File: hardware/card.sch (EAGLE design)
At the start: 56 parts, among them J1 UE27AC54100, J2 B2PS-VH(LF)(SN), J3 MINI-USB-UX60A-MB-5ST, J4 MICROSD, U1 ATSAMD21J_QFN, U3 TLV70233DBVR, U4 ATWINC1500_MR210PA, U5 NHD-C12832A1Z-FSW-FBW-3V3, U6 MIC2288YD5-TR, X3 32.768

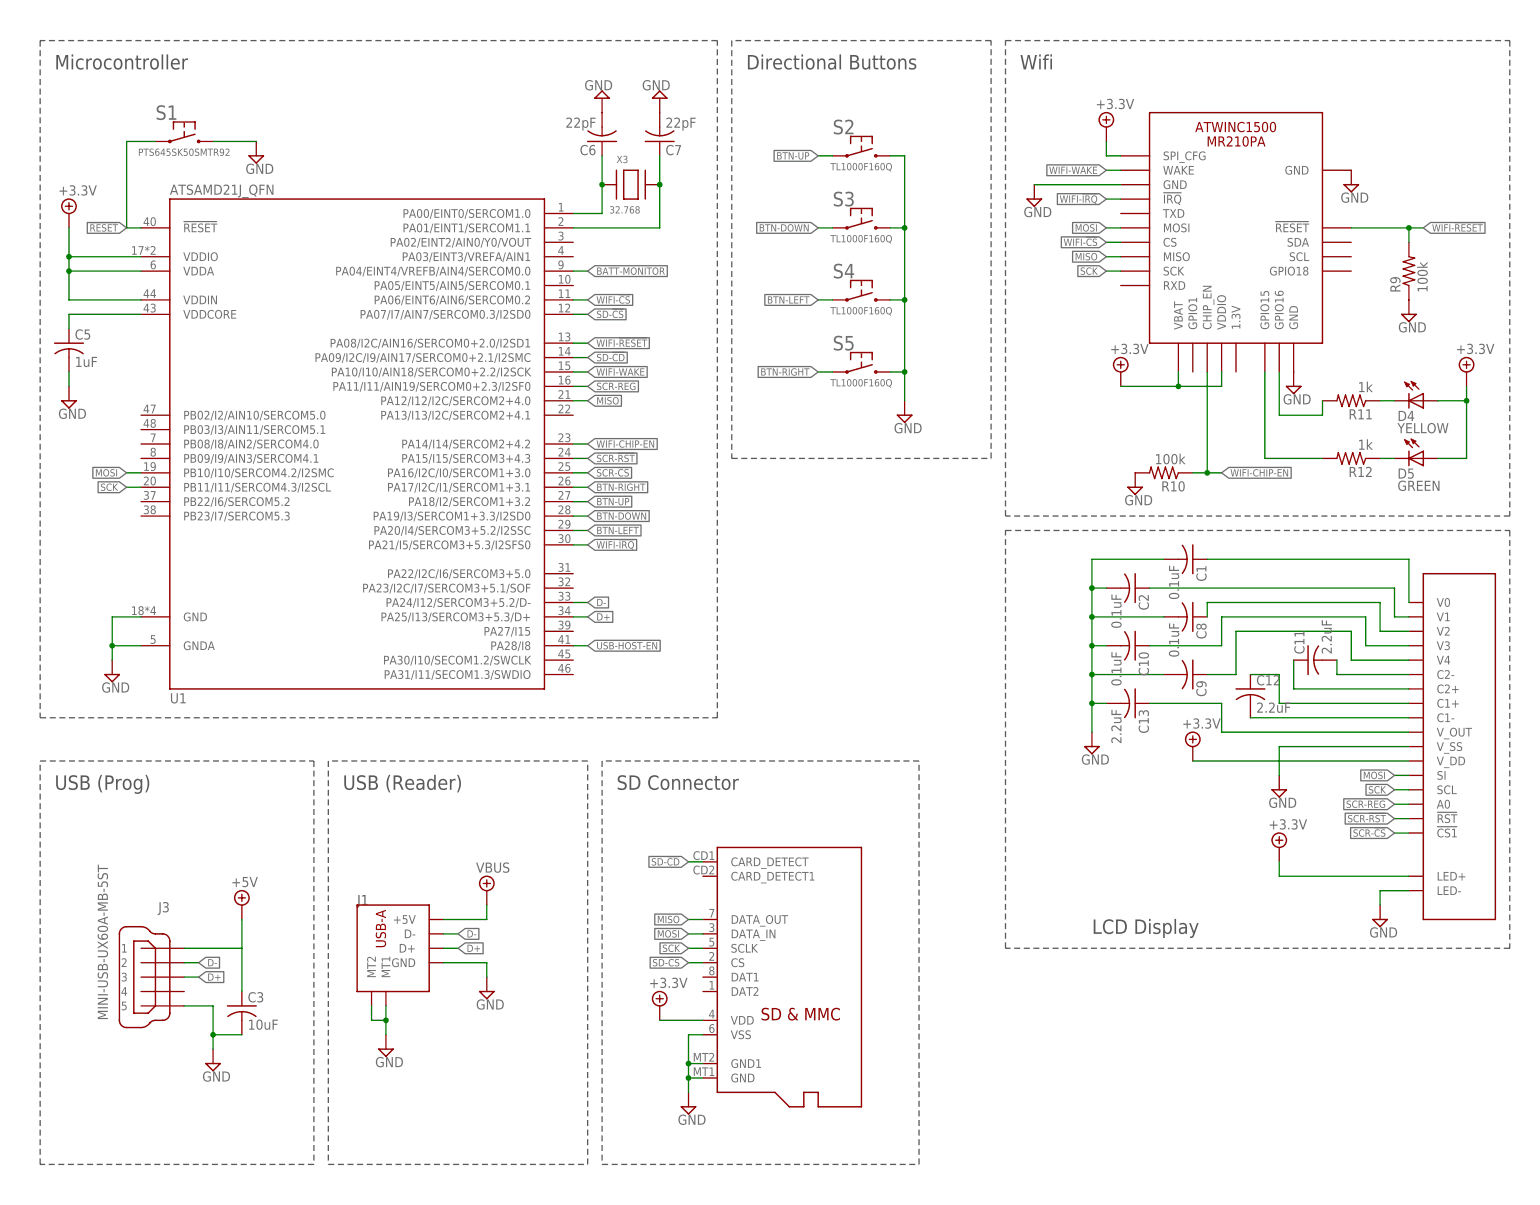
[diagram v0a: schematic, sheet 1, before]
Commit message: add framing for software components. Design review schematic tweaks
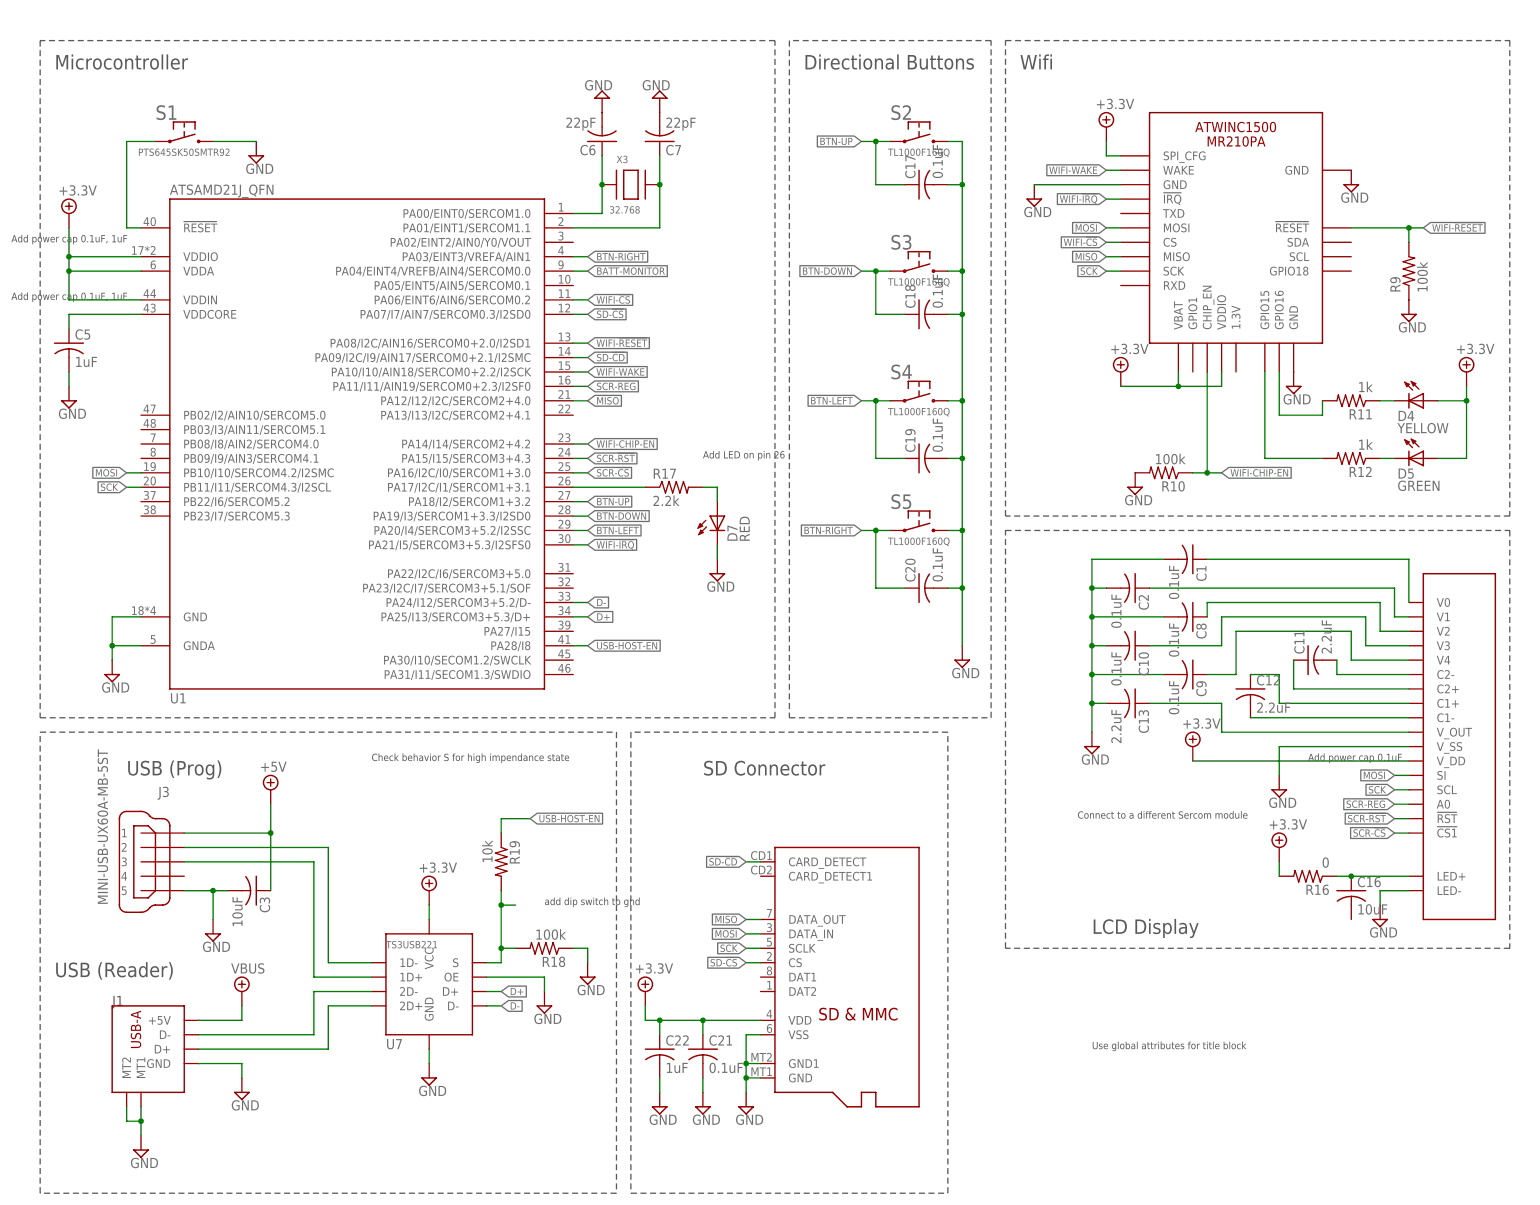
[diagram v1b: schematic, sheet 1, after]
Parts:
- removed CN1: (no value), lib-card:JST_2PIN
- removed T1: (no value), CardReader:BSS138
- added C16, C23, C24: 10uF, rcl:C-USC0603
- added C17, C18, C19, C20, C21: 0.1uF, rcl:C-USC0603
- added C22, C25, C26, C27: 1uF, rcl:C-USC0603
- added D7: RED, led:LED
- added F1: 2A, RoboJackets-Fuses:CHIP_FUSE0603
- added F2: 500mA, RoboJackets-Fuses:CHIP_FUSE0603
- added J5: JST_2PIN, CardReader:JST_2PIN
- added R17: 2.2k, RoboJackets-Resistors:R0603W
- added R18: 100k, RoboJackets-Resistors:R0603W
- added R19: 10k, RoboJackets-Resistors:R0603W
- added U7: TS3USB221, CardReader:TS3USB221
- C14: value 4.7uF -> 10uF
- C15: value 22uF -> 10uF
- C9: value (none) -> 0.1uF
- J4: device lib-card:MICROSD -> CardReader:MICROSD
- R1, R2, R3: value 150 -> 330
- R16: value 10k -> 0; device rcl:R-US_R0603 -> RoboJackets-Resistors:R0603W
- R6, R8: value 100k 1% -> 10k 1%
- U1: device lib-card:ATSAMD21J_QFN -> CardReader:ATSAMD21J_QFN
- U2: value (none) -> MCP73833; device lib-card:MCP73833 -> CardReader:MCP73833
- U4: device lib-card:ATWINC1500_MR210PA -> CardReader:ATWINC1500_MR210PA
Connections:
- removed net BOOST_ENABLE: R16.1, T1.D, U6.EN
- new net 1D+: J3.3, U7.1D+
- new net 1D-: J3.2, U7.1D-
- new net 2D+: J1.D+, U7.2D+
- new net 2D-: J1.D-, U7.2D-
- new net BATT-PRE-FUSE: F1.2, J5.1
- new net N$11: C16.1, R16.PIN1, U5.LED+
- new net N$13: R18.PIN2, R19.PIN2, U7.S
- new net PROG-LED: D7.A, R17.PIN2
- new net PROG-LED-2: R17.PIN1, U1.PA17/I2C/I1/SERCOM1+3.1
- net +3.3V: now also C21.1, C22.1, R16.PIN2, U7.VCC; no longer U5.LED+
- net +5V: now also C26.1, C3.1, J3.1; no longer T1.G
- net BATT: now also C27.2, F1.1; no longer CN1.1
- net BTN-DOWN: now also C18.1
- net BTN-LEFT: now also C19.1
- net BTN-RIGHT: now also C20.1, U1.PA03/EINT3/VREFA/AIN1; no longer U1.PA17/I2C/I1/SERCOM1+3.1
- net BTN-UP: now also C17.1
- net D+: now also U7.D+; no longer J1.D+, J3.3
- net D-: now also U7.D-; no longer J1.D-, J3.2
- net GND: now also C17.2, C18.2, C19.2, C20.2, C21.2, C22.2, C23.2, C24.2, C25.2, C26.2, C27.1, D7.C, J5.2, R18.PIN1, U7.GND, U7.OE; no longer CN1.2, T1.S
- net N$27: now also U5.C1+
- net N$29: now also C15.1, C23.1, C24.1, D6.C, F2.1, R14.2; no longer C3.1, J3.1
- net USB-HOST-EN: now also R19.PIN1
- net VBATT: now also C25.1, U6.EN; no longer R16.2
- net VBUS: now also F2.2; no longer C15.1, D6.C, R14.2
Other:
- note added: "Add LED on pin 26"
- note added: "Add power cap 0.1uF"
- note added: "Add power cap 0.1uF, 1uF"
- note added: "Add test points"
- note added: "Check behavior S for high impendance state"
- note added: "Connect to a different Sercom module"
- note added: "Use global attributes for title block"
- note added: "add dip switch to gnd"
- note added: "add power LEDS"
- note removed: "Potentially respec Add zener for Vcc and add +5v"
- moved on the sheet: C15, C3, D1, D2, D3, J1, J2, J3, R13, R3, S2, S3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

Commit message: Schematic Finished
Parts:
- removed U5: NHD-C12832A1Z-FSW-FBW-3V3, CardReader:NHD-C12832A1Z-FSW-FBW-3V3
- added C28, C29, C30, C32: 0.1uF, rcl:C-USC0603
- added C31: 1uF, rcl:C-USC0603
- added J6: 0541323062, CardReader:0541323062
- added J7: JST_2PIN, card:JST_2PIN
- added S6: KAE01SGGT, CardReader:KAE01SGGT
- C1, C10, C2, C8: value 0.1uF -> 1uF
- C11, C12, C13: value 2.2uF -> 0.1uF
- C16: value 10uF -> 1uF
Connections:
- removed net N$11: C16.1, R16.PIN1, U5.LED+
- removed net N$13: R18.PIN2, R19.PIN2, U7.S
- removed net N$19: C1.1, U5.V0
- removed net N$20: C8.1, U5.V2
- removed net N$21: C10.1, U5.V3
- removed net N$22: C2.1, U5.V1
- removed net N$23: C9.1, U5.V4
- removed net N$24: C11.1, U5.C2+
- removed net N$25: C11.2, U5.C2-
- removed net N$26: C13.1, U5.V_OUT
- removed net N$27: C12.1, U5.C1+
- removed net N$28: C12.2, U5.C1-
- removed net SCR-!CS: U1.PA16/I2C/I0/SERCOM1+3.0, U5.!CS1
- removed net SCR-!RST: U1.PA15/I15/SERCOM3+4.3, U5.!RST
- removed net SCR-REG: U1.PA11/I11/AIN19/SERCOM0+2.3/I2SF0, U5.A0
- new net LCD-!CS: J6.1, U1.PA20/I4/SERCOM3+5.2/I2SSC
- new net LCD-!RES: J6.2, U1.PA22/I2C/I6/SERCOM3+5.0
- new net LCD-A0: J6.3, U1.PB03/I3/AIN11/SERCOM5.1
- new net LCD-CA1+: C2.1, J6.18
- new net LCD-CA1-: C1.2, C2.2, J6.17
- new net LCD-CA2+: C8.1, J6.19
- new net LCD-CA2-: C8.2, J6.20
- new net LCD-CA3+: C1.1, J6.16
- new net LCD-K: J7.2, R16.PIN1
- new net LCD-MOSI: J6.13, U1.PB22/I6/SERCOM5.2
- new net LCD-SCK: J6.12, U1.PB23/I7/SERCOM5.3
- new net LCD-V0: C28.1, J6.27
- new net LCD-V1: C13.1, J6.26
- new net LCD-V2: C12.1, J6.25
- new net LCD-V3: C11.1, J6.24
- new net LCD-V4: C9.1, J6.23
- new net LCD-VOUT: C10.1, J6.15
- new net USB-S: R18.PIN2, R19.PIN2, S6.1, U7.S
- net +3.3V: now also C16.1, C29.1, C30.1, C31.1, C32.1, J6.22, J6.4, J6.5, J7.1; no longer R16.PIN2, U5.V_DD
- net BTN-LEFT: now also U1.PA16/I2C/I0/SERCOM1+3.0; no longer U1.PA20/I4/SERCOM3+5.2/I2SSC
- net BTN-RIGHT: now also U1.PA15/I15/SERCOM3+4.3; no longer U1.PA03/EINT3/VREFA/AIN1
- net GND: now also C11.2, C12.2, C16.2, C28.2, C29.2, C30.2, C31.2, C32.2, J6.10, J6.11, J6.14, J6.21, J6.29, J6.30, J6.6, J6.7, J6.8, J6.9, R16.PIN2, S6.2; no longer C1.2, C2.2, C8.2, U5.LED-, U5.V_SS
- net MOSI: no longer U5.SI
- net SCK: no longer U5.SCL
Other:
- note added: "!RES"
- note added: "A0"
- note added: "C86"
- note added: "CAP1+"
- note added: "CAP1-"
- note added: "CAP2+"
- note added: "CAP2-"
- note added: "CAP3+"
- note added: "CS1B"
- note added: "DB0"
- note added: "DB1"
- note added: "DB2"
- note added: "DB3"
- note added: "DB4"
- note added: "DB5"
- note added: "DB6/SCL"
- note added: "DB7/SI"
- note added: "E"
- note added: "LCD Backlight"
- note added: "PS"
- note added: "R/W"
- note added: "V0"
- note added: "V1"
- note added: "V2"
- note added: "V3"
- note added: "V4"
- note added: "VDD"
- note added: "VOUT"
- note added: "VR(NC)"
- note added: "VSS"
- note removed: "Add LED on pin 26"
- note removed: "Add power cap 0.1uF"
- note removed: "Add power cap 0.1uF, 1uF"
- note removed: "Check behavior S for high impendance state"
- note removed: "Connect to a different Sercom module"
- note removed: "add dip switch to gnd"
- moved on the sheet: C1, C10, C11, C12, C13, C16, C2, C5, C6, C7, C8, C9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

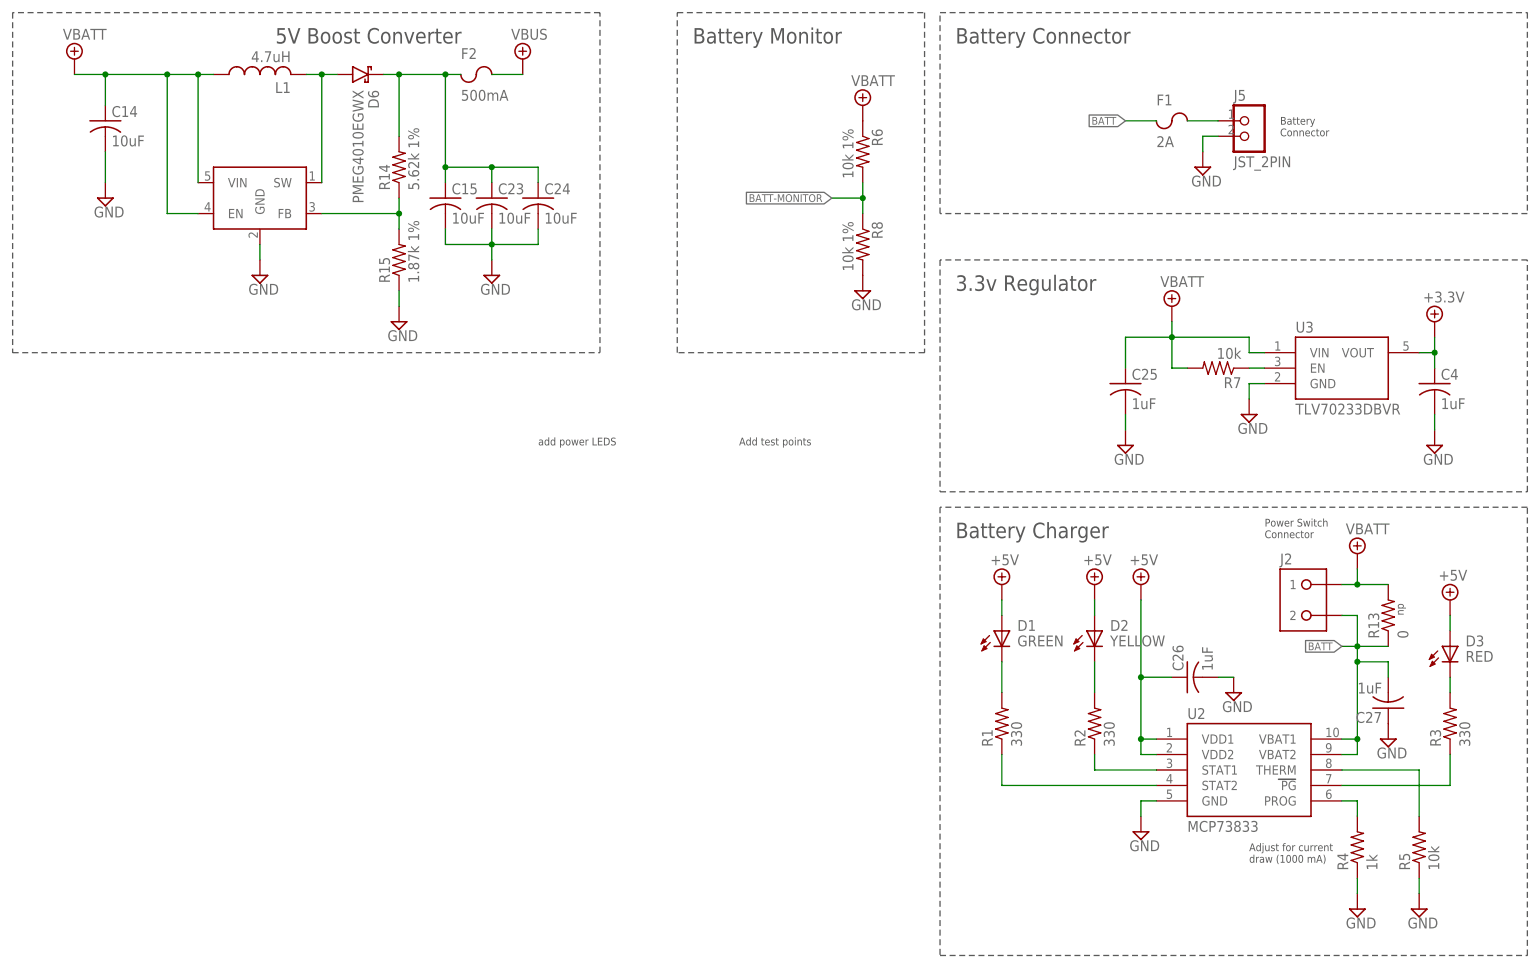
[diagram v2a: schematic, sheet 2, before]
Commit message: Added power test points and LEDs
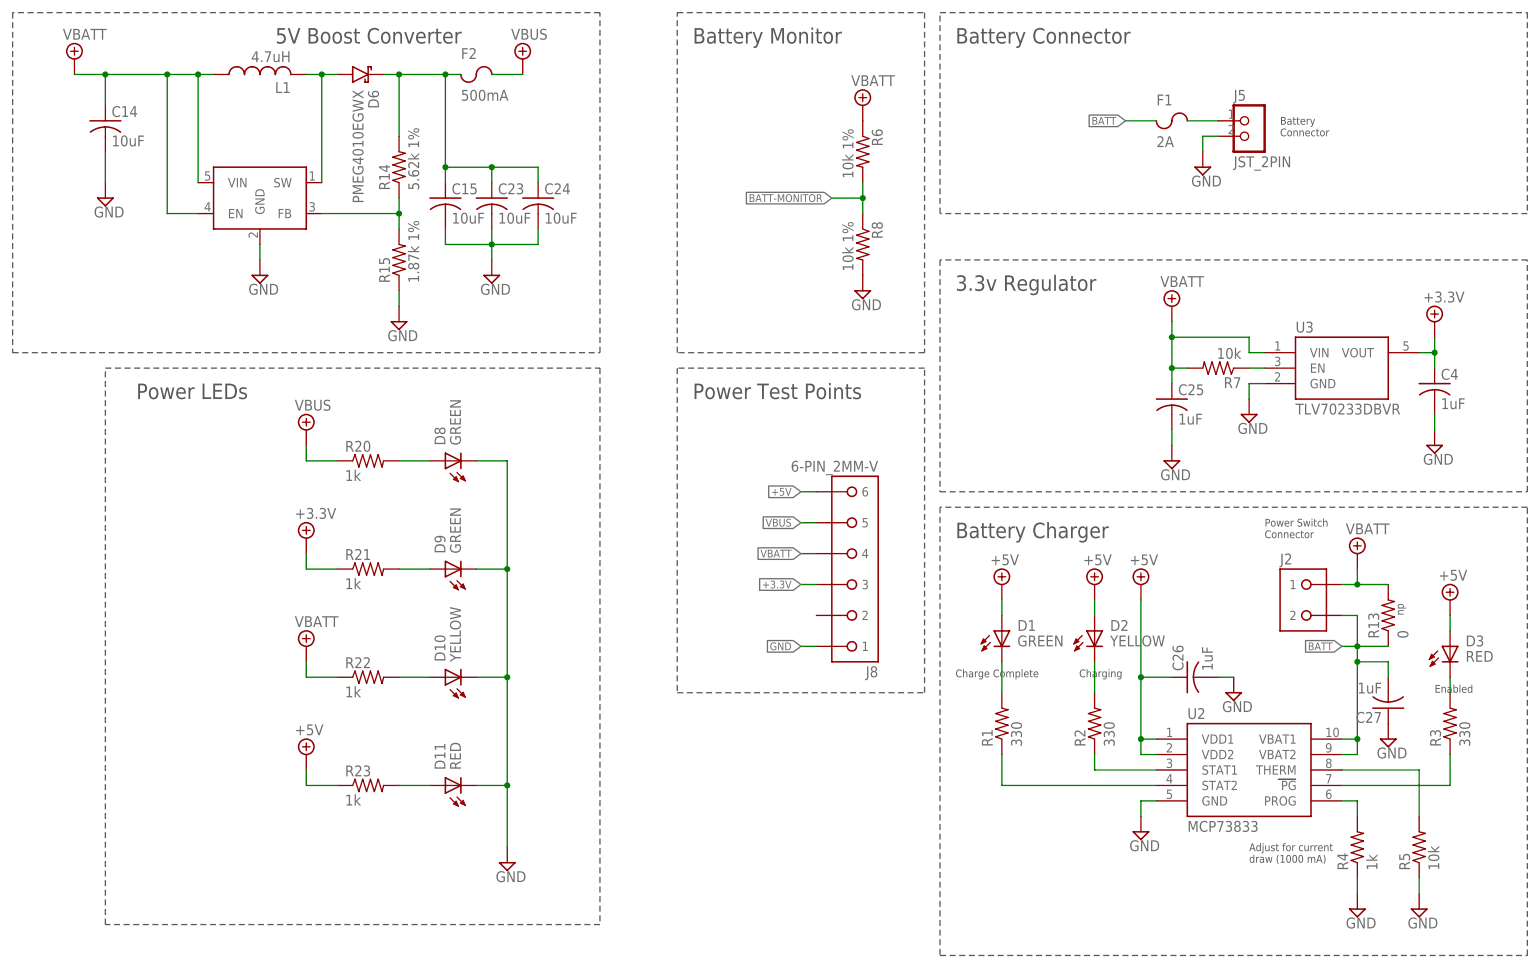
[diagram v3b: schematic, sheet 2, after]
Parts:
- added D10: YELLOW, lib-card:LED-SMD-GREEN
- added D11: RED, lib-card:LED-SMD-GREEN
- added D8, D9: GREEN, lib-card:LED-SMD-GREEN
- added J8: 6-PIN_2MM-V, RoboJackets-Connectors:6-PIN_2MM-V
- added R20, R21, R22, R23: 1k, rcl:R-US_R0603
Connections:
- net N$1 renamed LED-STAT2
- net N$14 renamed VDDCORE
- net N$15 renamed X3-1
- net N$16 renamed X3-2
- net N$17 renamed WIFI-LED-Y
- net N$18 renamed WIFI-LED-G
- net N$2 renamed LED-STAT1
- net N$29 renamed BOOST_OUTPUT
- net N$6 renamed LED-!PG
- new net LED-3V3: D9.A, R21.2
- new net LED-5V: D11.A, R23.2
- new net LED-VBATT: D10.A, R22.2
- new net LED-VBUS: D8.A, R20.2
- net +3.3V: now also J8.3, R21.1
- net +5V: now also J8.6, R23.1
- net GND: now also D10.K, D11.K, D8.K, D9.K, J8.1
- net VBATT: now also J8.4, R22.1
- net VBUS: now also J8.5, R20.1
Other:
- note added: "Charge Complete"
- note added: "Charging"
- note added: "Enabled"
- note added: "Power LEDs"
- note added: "Power Test Points"
- note removed: "Add test points"
- note removed: "Use global attributes for title block"
- note removed: "add power LEDS"
- moved on the sheet: C25
